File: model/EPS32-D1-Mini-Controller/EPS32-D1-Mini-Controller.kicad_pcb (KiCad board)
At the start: 2 copper layers, 98.2 x 54.9 mm, 27 parts, among them J1 Buck Converter, J2 I2C, J3 LED Channel 1, J4 LED Channel 2, J5 LED Channel 3, J6 LED Channel 4, J7 5V/12V Power, J8 I2C, J9 Barrel_Jack, U1 esp32-wemos-d1-mini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

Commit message: updates
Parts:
- added ?: , , F.Cu at (49.8, 50.2)
- added ?: , , F.Cu at (46.4, 50.2)
- moved U3 22.2 mm to (80.6, 40.0)
- moved U4 19.1 mm to (80.6, 62.2)
- moved J7 9.59 mm to (34.2, 34.7), turned to -90 degrees
- moved C2 8.35 mm to (73.7, 78.7)
- moved C1 4.96 mm to (78.3, 79.4)
- moved J9 3.04 mm to (36.5, 50.5)
- moved F1 2.73 mm to (49.8, 36.9)
- moved J1 2.54 mm to (62.2, 39.0)
- moved J3 1.69 mm to (119.5, 45.3)
- moved J4 0.95 mm to (119.5, 55.6)
- moved J6 0.55 mm to (119.5, 76.3)
- moved J5 0.22 mm to (119.5, 66.0)
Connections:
- J9 pad 1: GND -> +VCC
- J9 pad 3: (no net) -> GND
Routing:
- net +12V: track 99.0 -> 0.00 mm, vias 6 -> 0
- net GND: track 96.7 -> 0.00 mm
- net +VCC: track 34.2 -> 0.00 mm
- net SENS-SCL: track 107.6 -> 136.5 mm, vias 1 -> 3
- net +3.3V: track 137.1 -> 108.3 mm
- net Net-(U4-2Y): track 23.8 -> 48.2 mm, vias 0 -> 4
- net SENS-SDA: track 106.3 -> 127.0 mm, vias 1 -> 7
- net Net-(U4-4Y): track 46.3 -> 25.8 mm, vias 0 -> 2
- net DATA1: track 54.8 -> 36.0 mm, vias 2 -> 1
- net Net-(U4-1Y): track 23.7 -> 42.1 mm, vias 0 -> 4
- net DATA4: track 57.1 -> 40.2 mm, vias 2 -> 0
- net DATA2: track 45.4 -> 30.3 mm, vias 2 -> 1
- net MIC_SD: track 44.2 -> 56.0 mm
- net +5V: track 94.0 -> 86.3 mm, vias 0 -> 1
- net Net-(U4-3Y): track 18.9 -> 26.5 mm, vias 0 -> 2
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- added copper zone on F.Cu, net +12V
- added copper zone on F.Cu, net +VCC
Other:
- board text added: "WayWayWay"

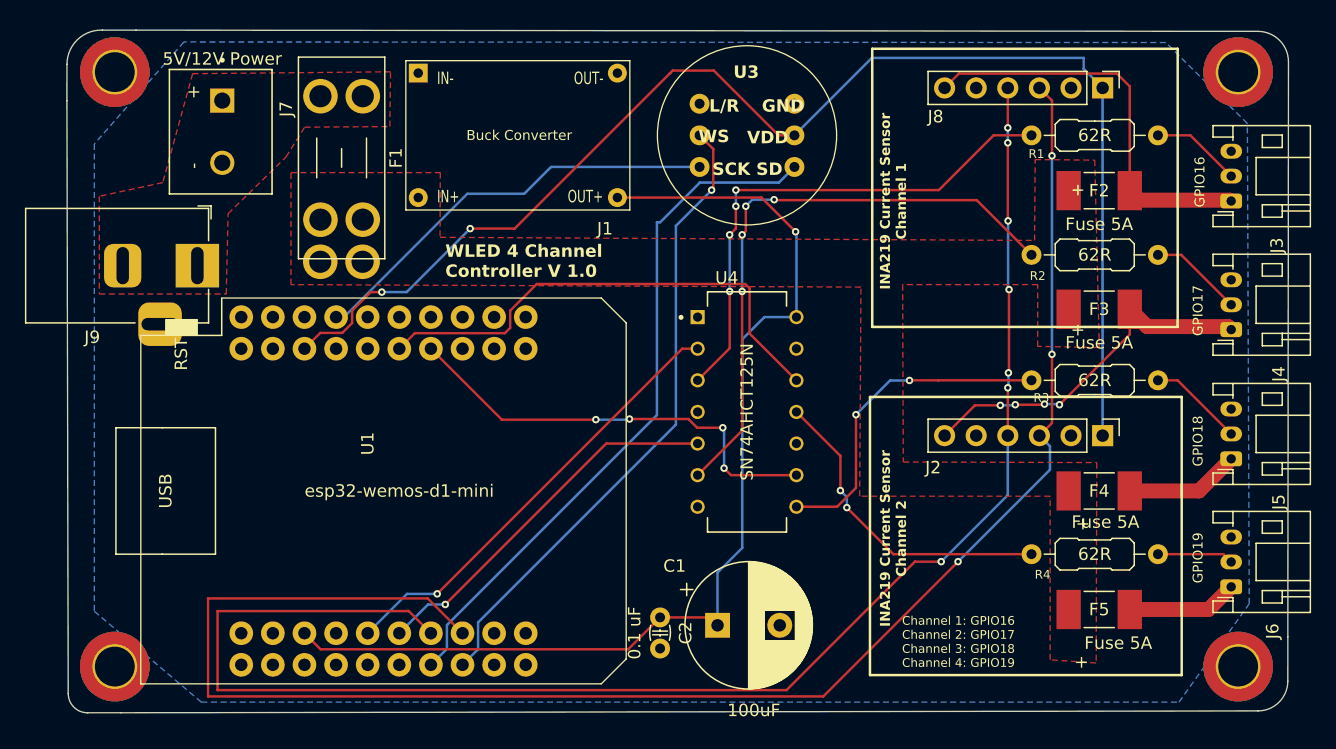
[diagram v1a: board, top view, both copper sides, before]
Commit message: fix barrell jack
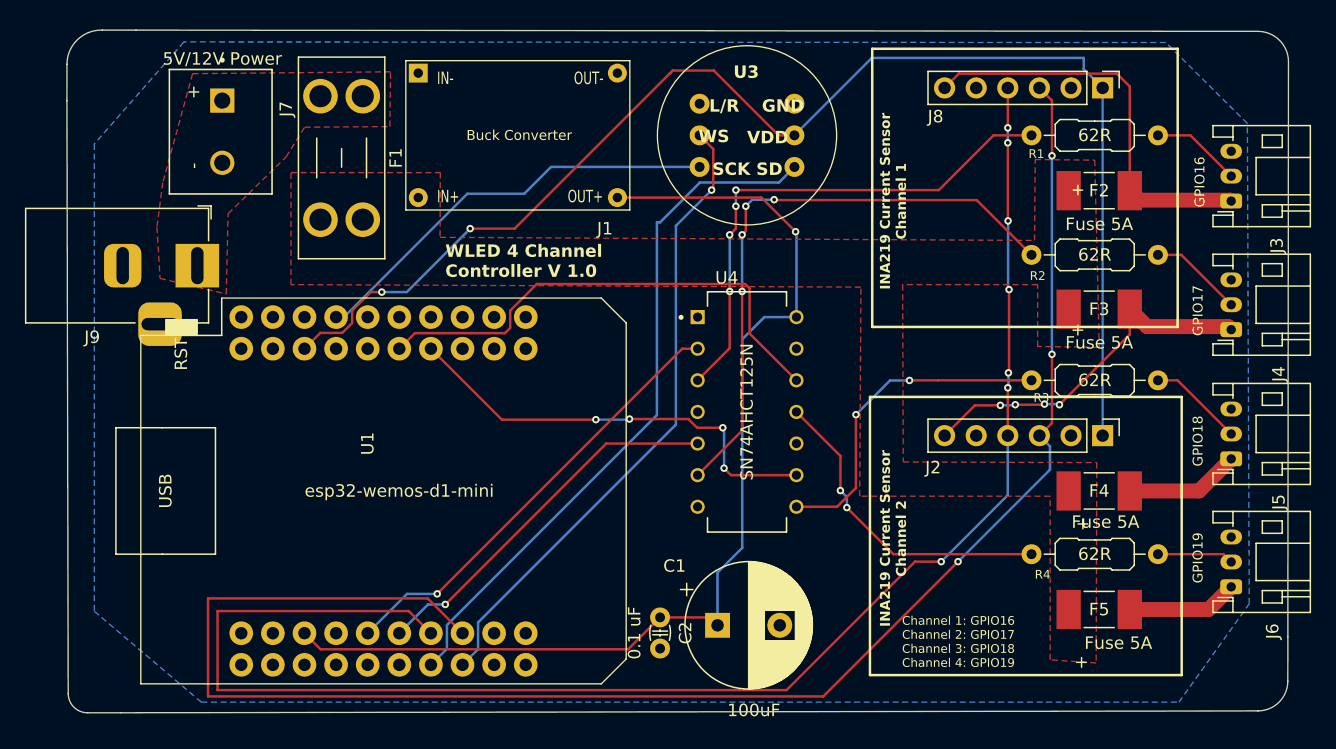
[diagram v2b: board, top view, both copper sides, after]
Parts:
- removed ? (x2): , 
- removed REF** (x4): MountingHole_3.2mm_M3_DIN965_Pad_TopBottom, MountingHole:MountingHole_3.2mm_M3_DIN965_Pad_TopBottom
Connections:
- J9 pad 2: +VCC -> GND
- J9 pad 3: GND -> (no net)

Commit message: updates
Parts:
- J3, J4, J5, J6: footprint Connector_JST:JST_PH_S3B-PH-K_1x03_P2.00mm_Horizontal -> TerminalBlock_Phoenix:TerminalBlock_Phoenix_MPT-0,5-3-2.54_1x03_P2.54mm_Horizontal
